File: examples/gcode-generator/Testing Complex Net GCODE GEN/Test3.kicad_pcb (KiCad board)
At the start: 2 copper layers, 100 x 60 mm, 10 parts, among them J1 Jack-DC, SW1 SW_Push, U1 Wave Gen, U2 LF356, U3 ESP-M2, U4 LD1117V33

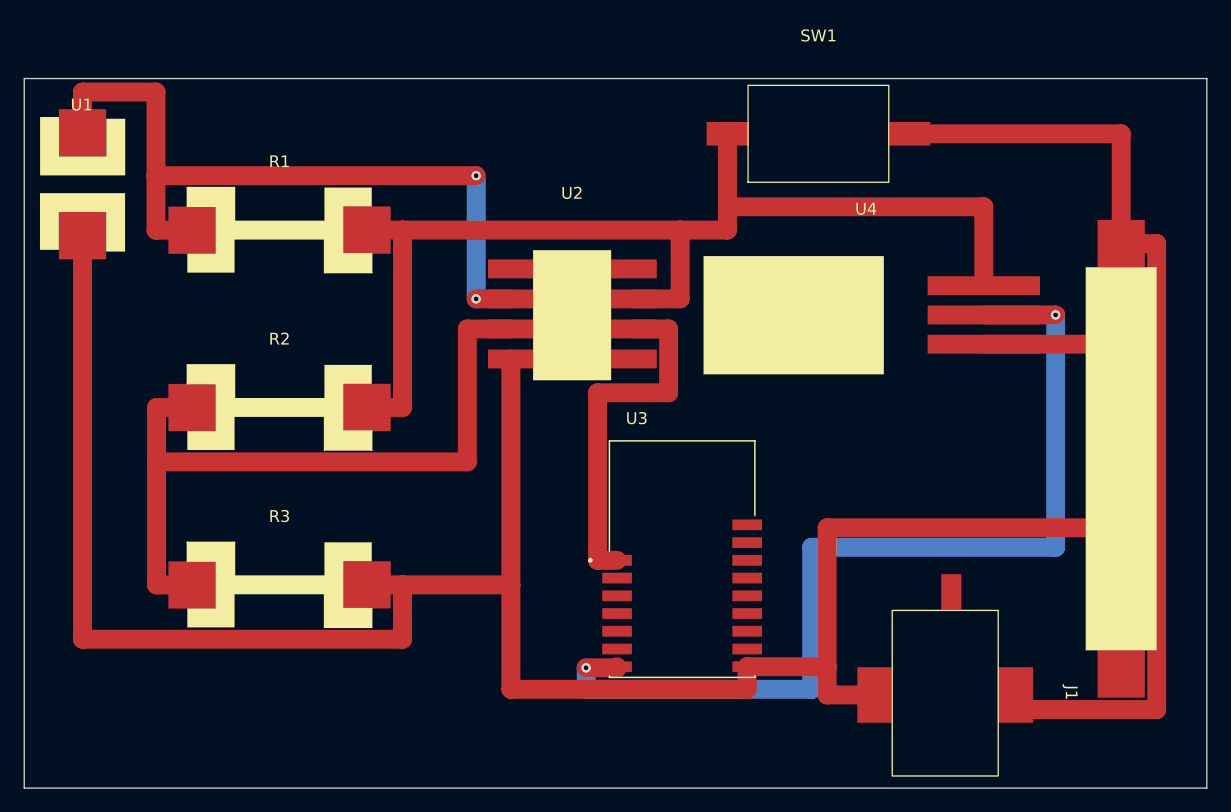
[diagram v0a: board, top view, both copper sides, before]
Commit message: Working version with double output layers, needs optimization in printing
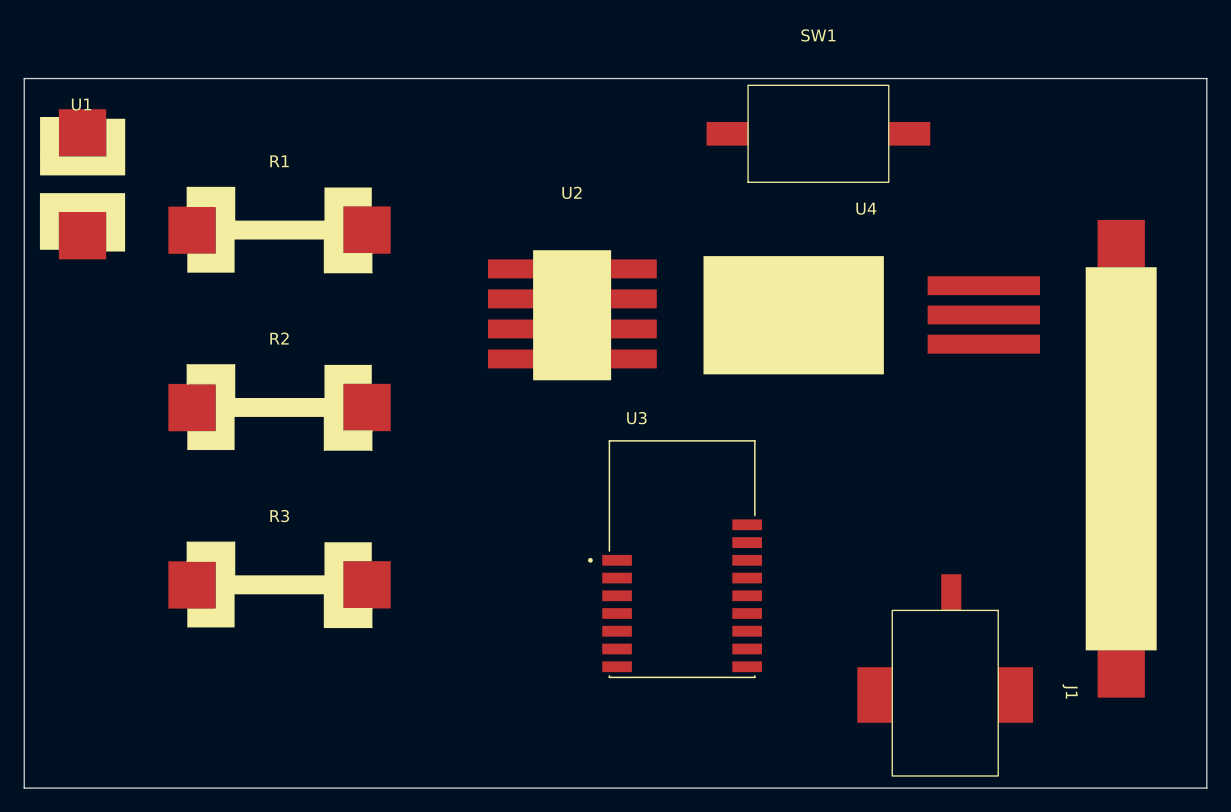
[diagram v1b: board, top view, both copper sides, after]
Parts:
- J1: value Jack-DC -> Barrel_Jack_Switch
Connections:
- J1 pad 3: (no net) -> Net-(BT1-Pad2)
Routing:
- net Net-(BT1-Pad2): track 217.1 -> 0.00 mm
- net Net-(R1-Pad2): track 94.7 -> 0.00 mm
- net Net-(BT1-Pad1): track 82.8 -> 0.00 mm
- net Net-(U3-Pad7): track 82.0 -> 0.00 mm, vias 2 -> 0
- net Net-(R1-Pad1): track 64.8 -> 0.00 mm, vias 2 -> 0
- net Net-(R2-Pad1): track 62.2 -> 0.00 mm
- net Net-(U2-Pad6): track 30.2 -> 0.00 mm
